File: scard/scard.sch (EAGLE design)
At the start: 70 parts, among them P1 TPS548A20, Q1 FDN360P, T1 LT3652, X1 COAX, X2 1365-20

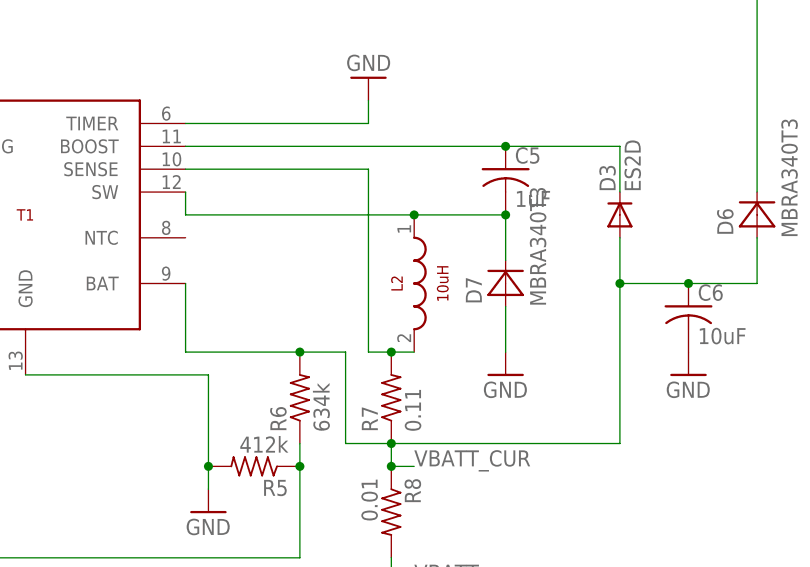
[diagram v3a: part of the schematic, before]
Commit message: added new 10uH inductor due to original inductor going out of stock. Updated CAM files. Fixed issue with GPS pads having no thermals
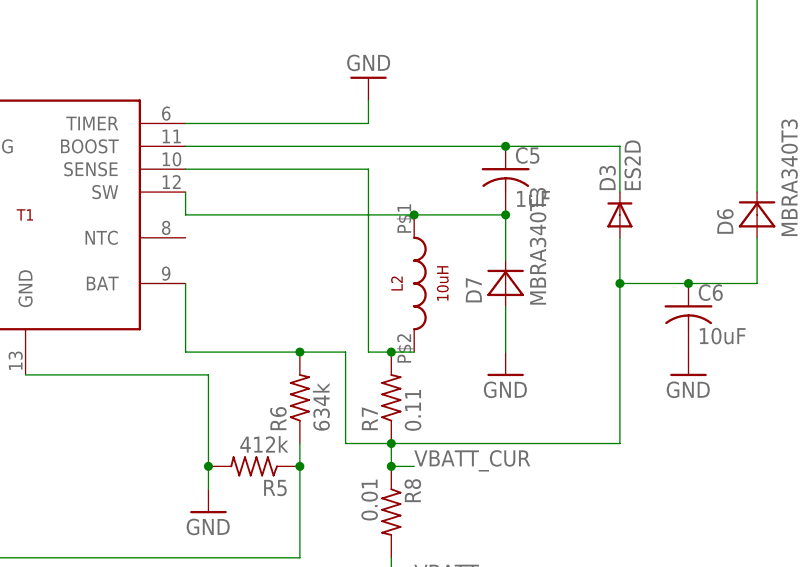
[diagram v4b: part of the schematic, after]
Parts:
- L2: device calsat:SRP7028A -> calsat:SRP7030-100M
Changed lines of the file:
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@@
 <?xml version="1.0" encoding="utf-8"?>
 <!DOCTYPE eagle SYSTEM "eagle.dtd">
-<eagle version="8.3.2">
+<eagle version="8.4.0">
 <drawing>
 <settings>
@@
 <part name="R7" library="rcl" library_urn="urn:adsk.eagle:library:334" deviceset="R-US_" device="R0603" package3d_urn="urn:adsk.eagle:package:23555/2" value="0.11"/>
 <part name="GND12" library="supply1" library_urn="urn:adsk.eagle:library:371" deviceset="GND" device=""/>
-<part name="L2" library="calsat" deviceset="SRP7028A" device="" value="10uH"/>
+<part name="L2" library="calsat" deviceset="SRP7030-100M" device="" value="10uH"/>
 <part name="R9" library="rcl" library_urn="urn:adsk.eagle:library:334" deviceset="R-US_" device="R0603" package3d_urn="urn:adsk.eagle:package:23555/2" value="0.01"/>
 <part name="R8" library="rcl" library_urn="urn:adsk.eagle:library:334" deviceset="R-US_" device="R0603" package3d_urn="urn:adsk.eagle:package:23555/2" value="0.01"/>
@@
 </segment>
 </net>
-<net name="N$4" class="0">
-<segment>
-<pinref part="T1" gate="G$1" pin="SW"/>
-<wire x1="-91.44" y1="-30.48" x2="-91.44" y2="-33.02" width="0.1524" layer="91"/>
-<pinref part="L2" gate="G$1" pin="@1"/>
-<wire x1="-91.44" y1="-33.02" x2="-66.04" y2="-33.02" width="0.1524" layer="91"/>
-<pinref part="C5" gate="G$1" pin="2"/>
-<wire x1="-66.04" y1="-33.02" x2="-55.88" y2="-33.02" width="0.1524" layer="91"/>
-<junction x="-66.04" y="-33.02"/>
-<junction x="-55.88" y="-33.02"/>
-<pinref part="D7" gate="G$1" pin="C"/>
-<wire x1="-55.88" y1="-38.1" x2="-55.88" y2="-33.02" width="0.1524" layer="91"/>
-</segment>
-</net>
 <net name="N$6" class="0">
 <segment>
 <pinref part="R7" gate="G$1" pin="2"/>
-<wire x1="-68.58" y1="-48.26" x2="-66.04" y2="-48.26" width="0.1524" layer="91"/>
-<pinref part="L2" gate="G$1" pin="@2"/>
 <pinref part="T1" gate="G$1" pin="SENSE"/>
 <wire x1="-91.44" y1="-27.94" x2="-71.12" y2="-27.94" width="0.1524" layer="91"/>
 <wire x1="-68.58" y1="-48.26" x2="-71.12" y2="-48.26" width="0.1524" layer="91"/>
 <wire x1="-71.12" y1="-48.26" x2="-71.12" y2="-27.94" width="0.1524" layer="91"/>
+<pinref part="L2" gate="G$1" pin="@2"/>
+<wire x1="-66.04" y1="-48.26" x2="-68.58" y2="-48.26" width="0.1524" layer="91"/>
 <junction x="-68.58" y="-48.26"/>
 </segment>
@@
 </segment>
 </net>
+<net name="N$18" class="0">
+<segment>
+<pinref part="T1" gate="G$1" pin="SW"/>
+<wire x1="-91.44" y1="-30.48" x2="-91.44" y2="-33.02" width="0.1524" layer="91"/>
+<pinref part="L2" gate="G$1" pin="@1"/>
+<pinref part="C5" gate="G$1" pin="2"/>
+<wire x1="-66.04" y1="-33.02" x2="-55.88" y2="-33.02" width="0.1524" layer="91"/>
+<junction x="-55.88" y="-33.02"/>
+<pinref part="D7" gate="G$1" pin="C"/>
+<wire x1="-55.88" y1="-38.1" x2="-55.88" y2="-33.02" width="0.1524" layer="91"/>
+<wire x1="-91.44" y1="-33.02" x2="-66.04" y2="-33.02" width="0.1524" layer="91"/>
+<junction x="-66.04" y="-33.02"/>
+</segment>
+</net>

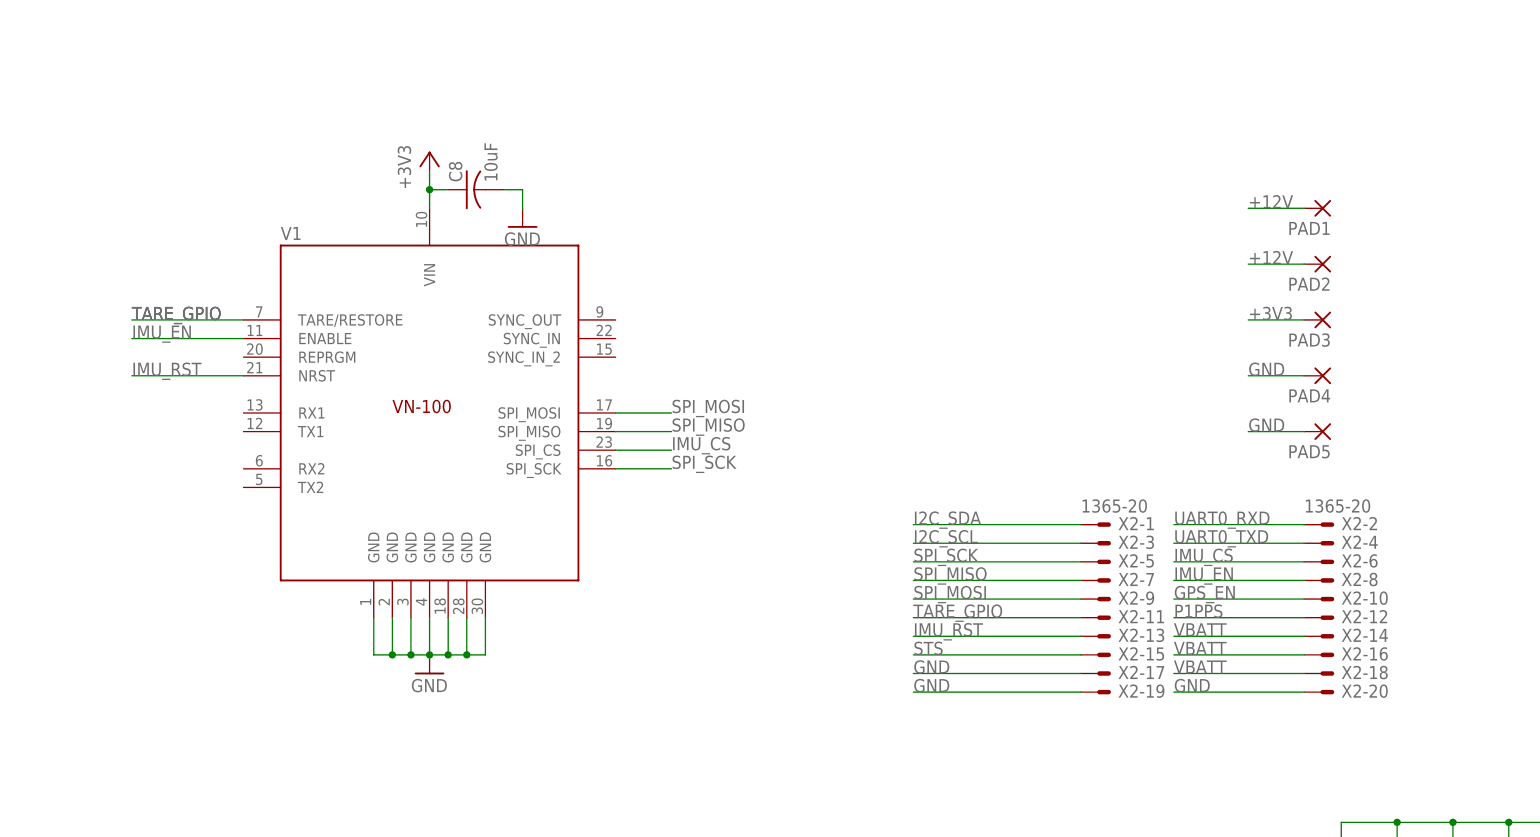
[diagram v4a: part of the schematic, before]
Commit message: Started v0.4 S Card moved gps far from power inductor reorganized battery charging circuit in preparation for routing
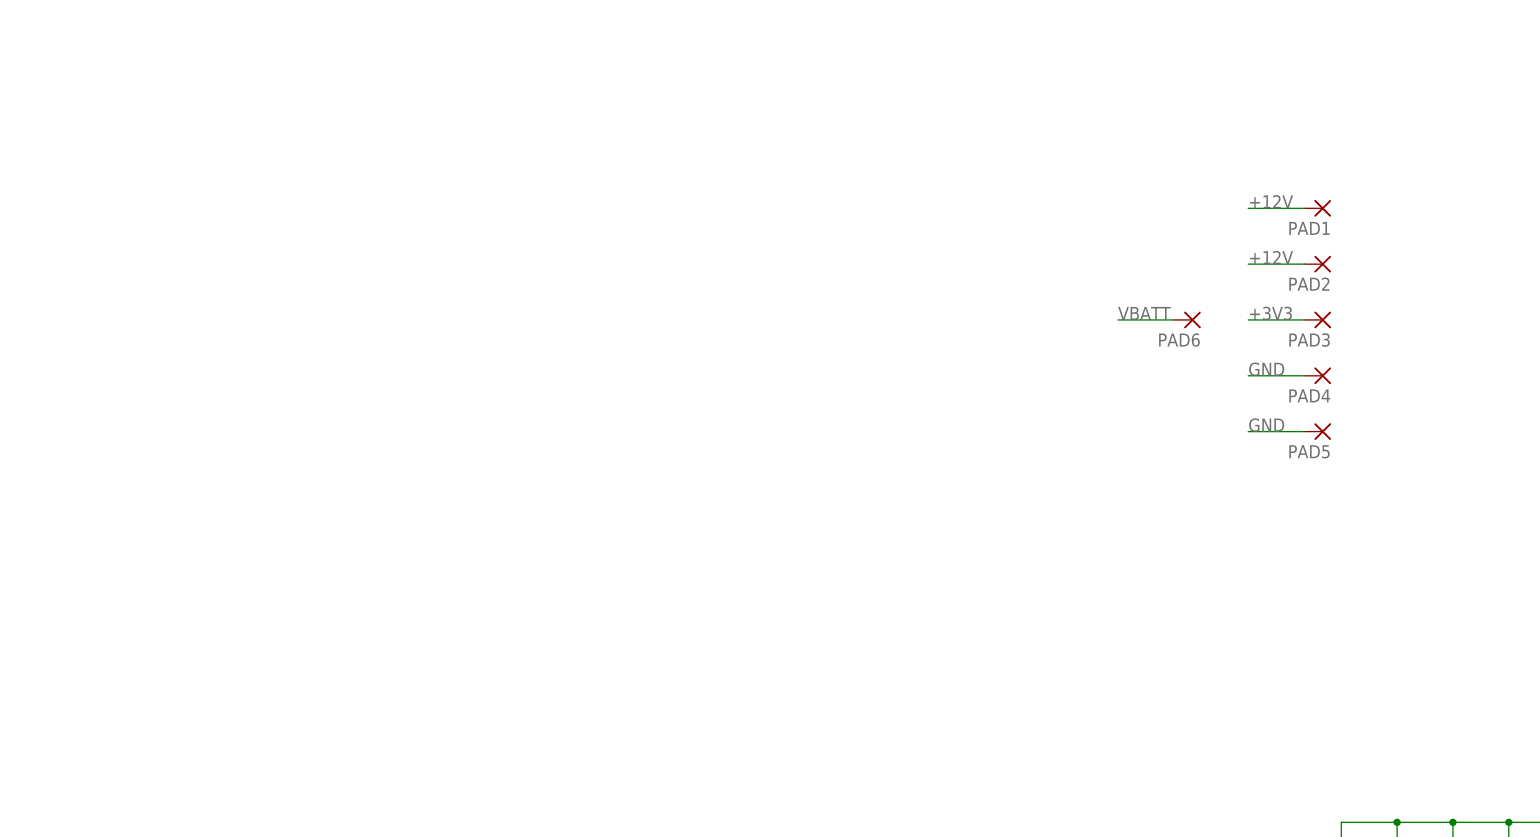
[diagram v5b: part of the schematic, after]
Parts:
- removed C8: 10uF, resistor:C-USC0603
- removed V1: VN100NORMAL, vectornav:VN100NORMAL
- removed X2: 1365-20, con-leotronics:1365-20
- added PAD6: (no value), wirepad:SMD5
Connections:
- removed net IMU_CS: V1.SPI_CS, X2-6.S
- removed net IMU_EN: V1.ENABLE, X2-8.S
- removed net IMU_RST: V1.NRST, X2-13.S
- removed net SPI_MISO: V1.SPI_MISO, X2-7.S
- removed net SPI_MOSI: V1.SPI_MOSI, X2-9.S
- removed net SPI_SCK: V1.SPI_SCK, X2-5.S
- removed net TARE_GPIO: V1.TARE/RESTORE, X2-11.S
- net +3V3: no longer C8.1, V1.VIN
- net GND: no longer C8.2, V1.GND@1, V1.GND@2, V1.GND@3, V1.GND@4, V1.GND@5, V1.GND@6, V1.GND@7, X2-17.S, X2-19.S, X2-20.S
- net GPS_EN: no longer X2-10.S
- net I2C_SCL: no longer X2-3.S
- net I2C_SDA: no longer X2-1.S
- net P1PPS: no longer X2-12.S
- net STS: no longer X2-15.S
- net UART0_RXD: no longer X2-2.S
- net UART0_TXD: no longer X2-4.S
- net VBATT: now also PAD6.P; no longer X2-14.S, X2-16.S, X2-18.S
